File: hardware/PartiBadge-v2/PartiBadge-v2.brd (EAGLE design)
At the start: 118.9 x 117.7 mm, 31 parts, among them IC2 TSMP58000, J1 I2C, J2 Supply, U1 1042

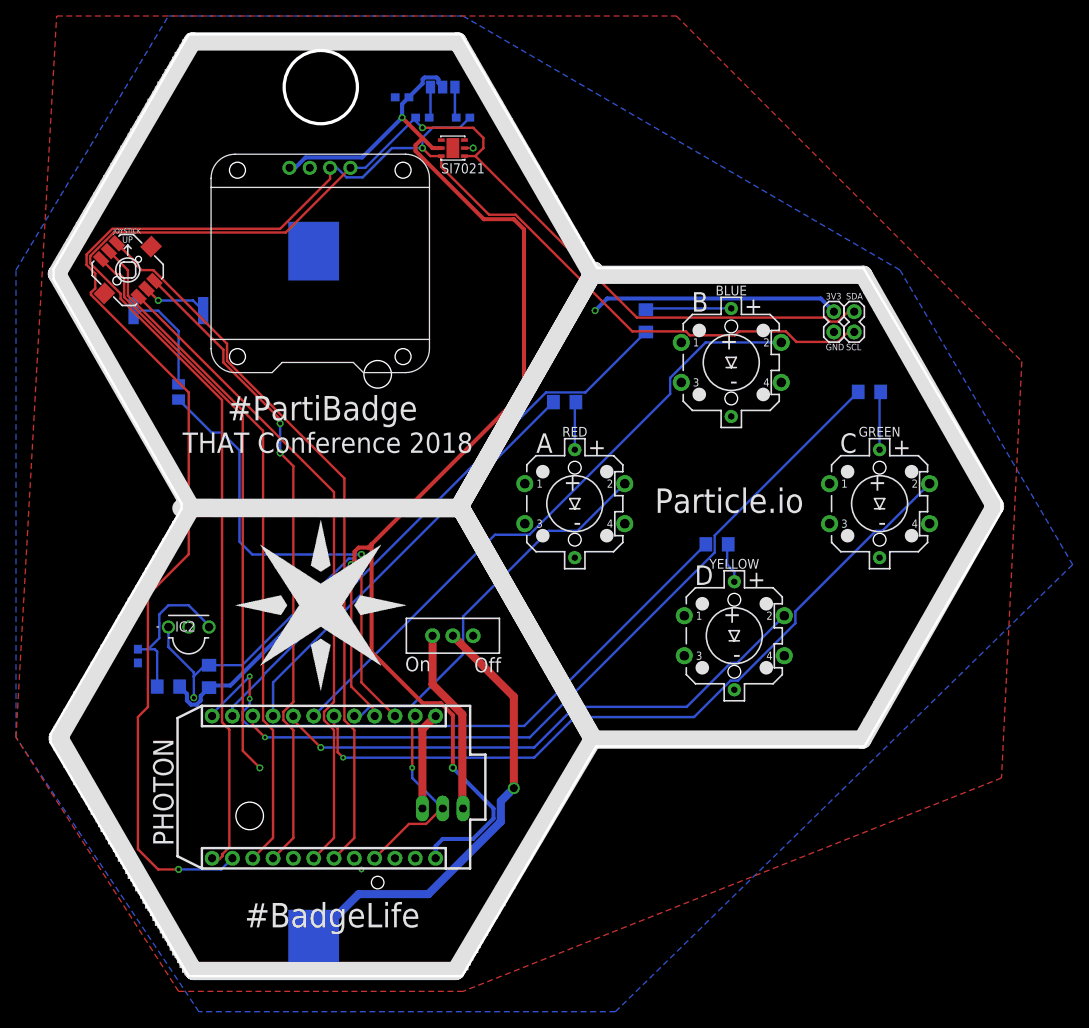
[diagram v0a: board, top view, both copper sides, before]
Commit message: updated schematic and layout based on feedback from Brett
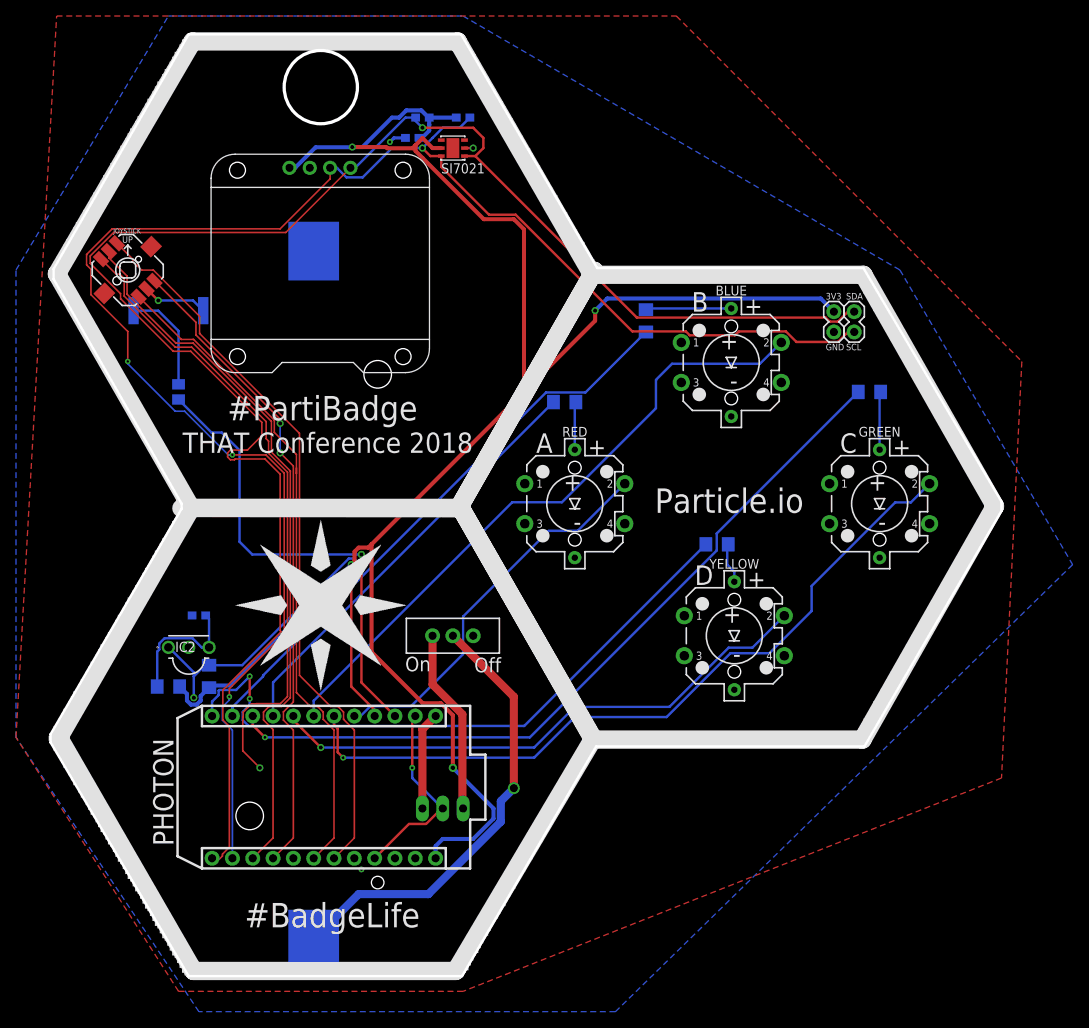
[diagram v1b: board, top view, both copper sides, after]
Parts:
- removed SJ1: (no value), jumper:SJ_2
- R7: value 100 -> 200
- moved C2 9.16 mm to (22.9, 48.3), turned to 0 degrees
- moved C1 5.24 mm to (49.5, 108.0)
- moved IC2 2.54 mm to (21.6, 45.7)
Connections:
- removed net N$11: R5.2, SJ1.3
- removed net N$12: R6.2, SJ1.1
- net +3V3: now also R5.2, R6.2; no longer SJ1.2
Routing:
- net +3V3: track 217.3 -> 237.8 mm
- net SDA: track 202.2 -> 217.0 mm
- net LEFT: track 85.1 -> 93.1 mm
- net CENT: track 85.4 -> 90.4 mm
- net SCL: track 219.4 -> 215.4 mm, vias 2 -> 4
- net N$12: track 3.88 -> 0.00 mm
- net N$11: track 3.88 -> 0.00 mm
- net N$9: track 19.8 -> 16.6 mm
- net IR_RECEIVER: track 57.9 -> 55.4 mm
- net GND: track 33.7 -> 35.8 mm, vias 3 -> 4
- net BUTTON_B: track 79.0 -> 81.0 mm
- net LED_Y: track 80.3 -> 81.6 mm
- net DOWN: track 82.4 -> 83.4 mm
- net BUTTON_G: track 94.0 -> 95.0 mm
- net UP: track 91.1 -> 91.6 mm

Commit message: additional layout tweaks
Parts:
- added D7: (no value), SparkFun-Connectors:1X01
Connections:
- new net D7: D7.1, PHOTON.20
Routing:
- net +3V3: track 237.8 -> 231.3 mm
- net D7: track 0.00 -> 6.04 mm
- net SDA: track 217.0 -> 218.5 mm
- net SCL: track 215.4 -> 216.2 mm
- net DOWN: track 83.4 -> 82.9 mm

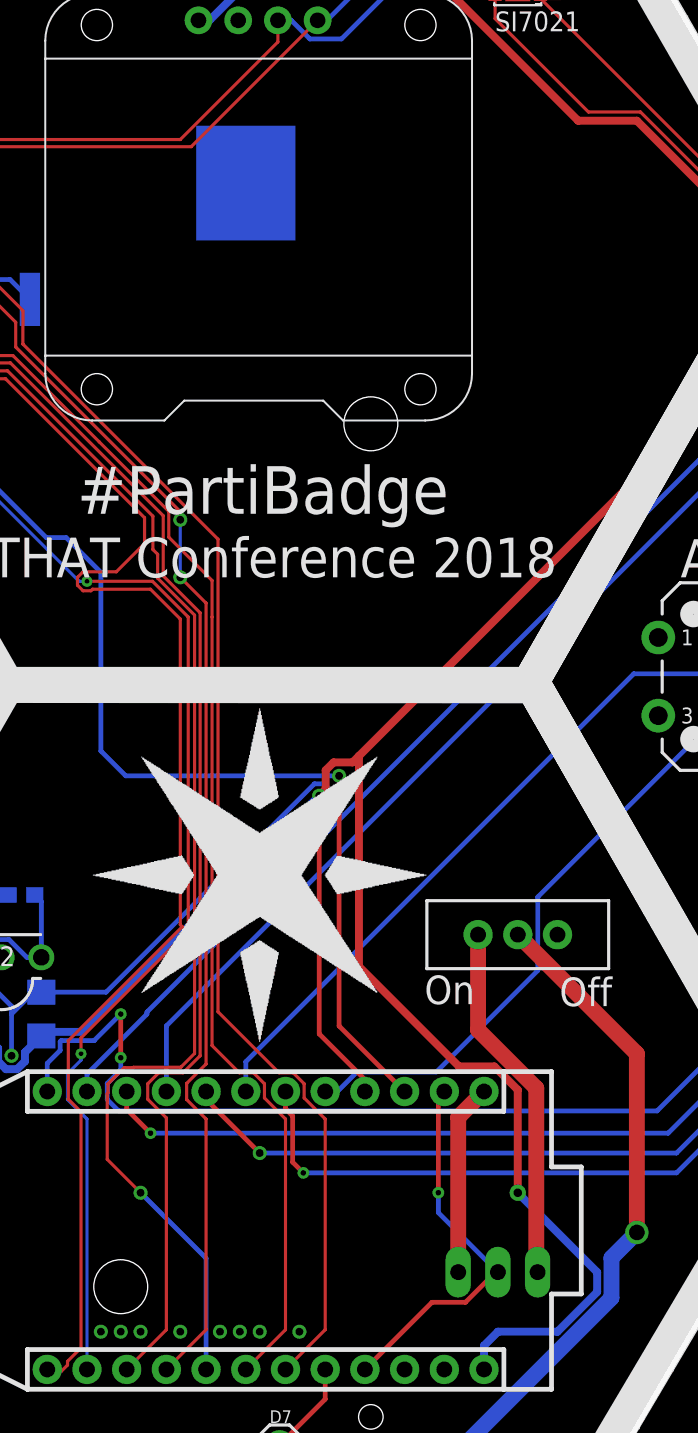
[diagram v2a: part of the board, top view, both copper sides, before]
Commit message: added vias for ground plane
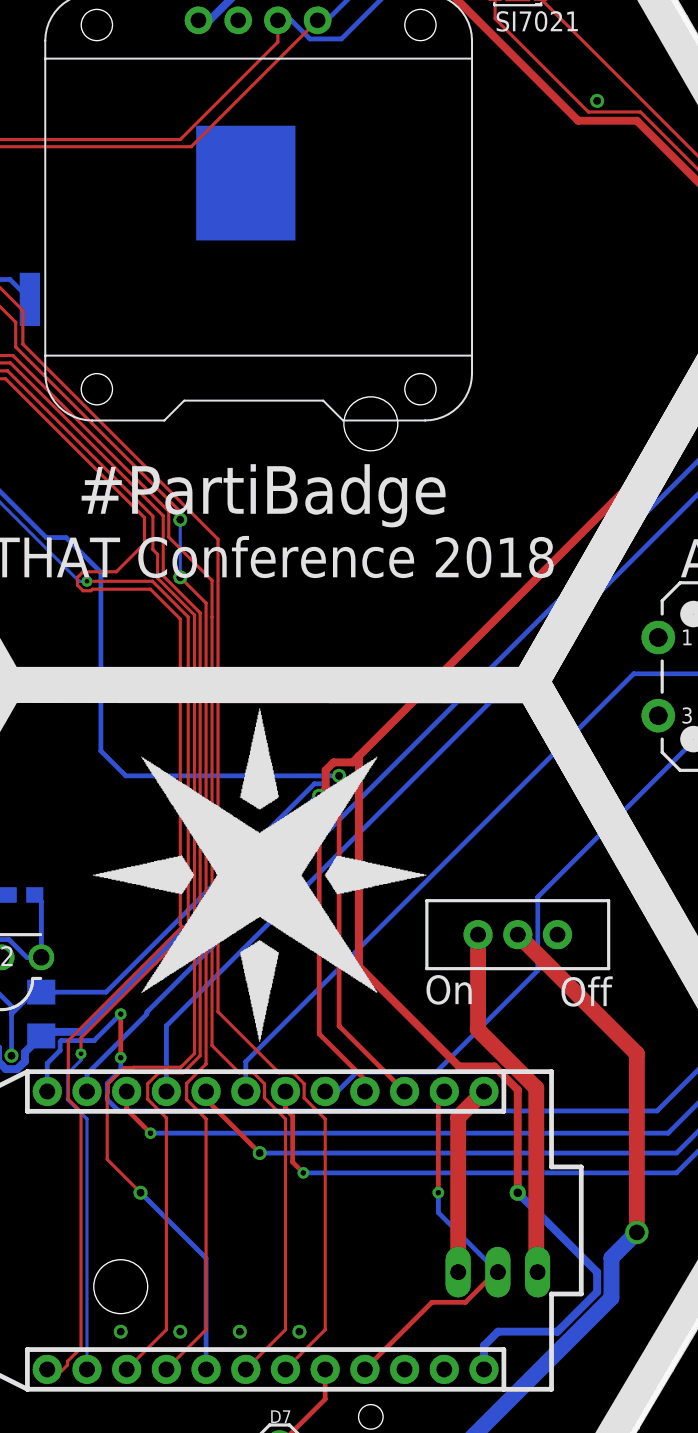
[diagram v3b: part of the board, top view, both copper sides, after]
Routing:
- net GND: vias 4 -> 9
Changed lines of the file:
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@@
 <drawing>
 <settings>
-<setting alwaysvectorfont="yes"/>
+<setting alwaysvectorfont="no"/>
 <setting verticaltext="up"/>
 </settings>
@@
 <wire x1="47.244" y1="107.95" x2="46.736" y2="107.442" width="0.4064" layer="16"/>
 <via x="46.736" y="107.442" extent="1-16" drill="0.35"/>
+<via x="29.21" y="20.32" extent="1-16" drill="0.5"/>
+<via x="33.02" y="20.32" extent="1-16" drill="0.5"/>
+<via x="36.83" y="20.32" extent="1-16" drill="0.5"/>
+<via x="40.64" y="20.32" extent="1-16" drill="0.5"/>
+<via x="59.69" y="99.06" extent="1-16" drill="0.5"/>
 </signal>
 <signal name="+3V3">
@@
 <contactref element="S5" pad="3"/>
 </signal>
-<signal name="N$2">
-<via x="27.94" y="20.32" extent="1-16" drill="0.5"/>
-</signal>
-<signal name="N$3">
-<via x="29.21" y="20.32" extent="1-16" drill="0.5"/>
-</signal>
-<signal name="N$6">
-<via x="30.48" y="20.32" extent="1-16" drill="0.5"/>
-</signal>
-<signal name="N$11">
-<via x="33.02" y="20.32" extent="1-16" drill="0.5"/>
-</signal>
-<signal name="N$12">
-<via x="35.56" y="20.32" extent="1-16" drill="0.5"/>
-</signal>
-<signal name="N$14">
-<via x="36.83" y="20.32" extent="1-16" drill="0.5"/>
-</signal>
-<signal name="N$15">
-<via x="38.1" y="20.32" extent="1-16" drill="0.5"/>
-</signal>
-<signal name="N$16">
-<via x="40.64" y="20.32" extent="1-16" drill="0.5"/>
-</signal>
 <signal name="D7">

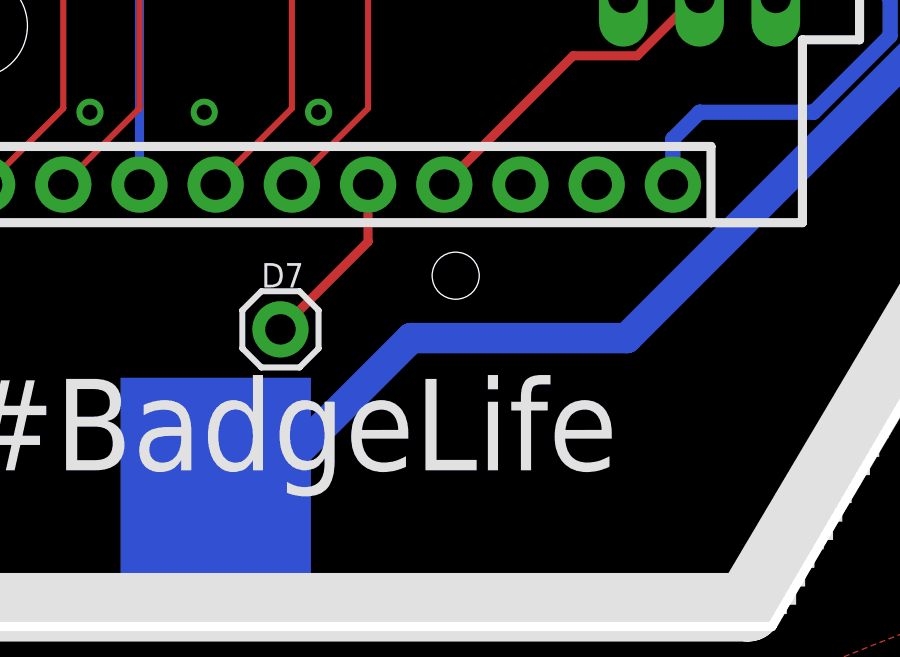
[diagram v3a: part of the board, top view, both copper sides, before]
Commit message: fix D7 breakout placement
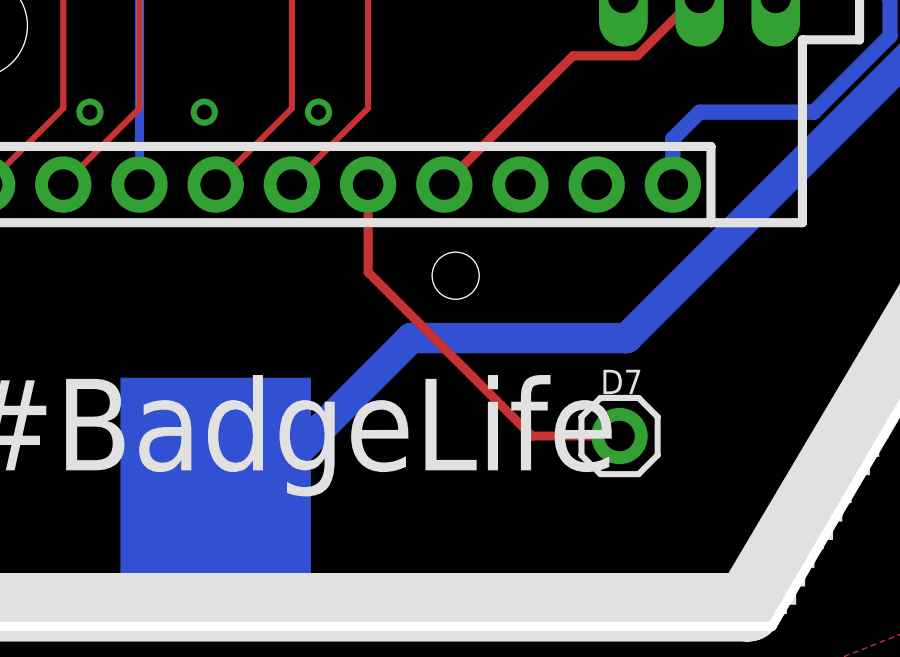
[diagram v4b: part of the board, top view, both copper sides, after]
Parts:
- R5, R6: value 4.7k -> 2.2k
- moved D7 11.8 mm to (50.7, 9.53)
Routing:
- net D7: track 6.04 -> 13.6 mm
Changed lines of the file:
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@@
 <drawing>
 <settings>
-<setting alwaysvectorfont="no"/>
+<setting alwaysvectorfont="yes"/>
 <setting verticaltext="up"/>
 </settings>
@@
 <attribute name="PROD_ID" value=" " x="87.63" y="57.15" size="1.778" layer="28" rot="MR180" display="off"/>
 </element>
-<element name="R5" library="SparkFun-Resistors" library_urn="urn:adsk.eagle:library:532" package="0603" package3d_urn="urn:adsk.eagle:package:39650/1" value="4.7k" x="50.8" y="110.49" rot="MR180">
+<element name="R5" library="SparkFun-Resistors" library_urn="urn:adsk.eagle:library:532" package="0603" package3d_urn="urn:adsk.eagle:package:39650/1" value="2.2k" x="50.8" y="110.49" rot="MR180">
 <attribute name="PROD_ID" value="RES-07857" x="50.8" y="110.49" size="1.778" layer="28" rot="MR180" display="off"/>
 </element>
-<element name="R6" library="SparkFun-Resistors" library_urn="urn:adsk.eagle:library:532" package="0603" package3d_urn="urn:adsk.eagle:package:39650/1" value="4.7k" x="55.88" y="110.49" rot="MR0">
+<element name="R6" library="SparkFun-Resistors" library_urn="urn:adsk.eagle:library:532" package="0603" package3d_urn="urn:adsk.eagle:package:39650/1" value="2.2k" x="55.88" y="110.49" rot="MR0">
 <attribute name="PROD_ID" value="RES-07857" x="55.88" y="110.49" size="1.778" layer="28" rot="MR0" display="off"/>
 </element>
@@
 <attribute name="RS_PRICE/STOCK" value="" x="37.211" y="50.8" size="1.778" layer="28" rot="MR270" display="off"/>
 </element>
-<element name="D7" library="SparkFun-Connectors" library_urn="urn:adsk.eagle:library:513" package="1X01" package3d_urn="urn:adsk.eagle:package:38028/1" value="" x="39.37" y="13.081" smashed="yes">
-<attribute name="NAME" x="38.735" y="14.478" size="0.8128" layer="25" font="vector" ratio="20"/>
-<attribute name="VALUE" x="38.1" y="11.557" size="0.6096" layer="27" font="vector" ratio="20" align="top-left"/>
+<element name="D7" library="SparkFun-Connectors" library_urn="urn:adsk.eagle:library:513" package="1X01" package3d_urn="urn:adsk.eagle:package:38028/1" value="" x="50.673" y="9.525" smashed="yes">
+<attribute name="NAME" x="50.038" y="10.922" size="0.8128" layer="25" font="vector" ratio="20"/>
+<attribute name="VALUE" x="49.403" y="8.001" size="0.6096" layer="27" font="vector" ratio="20" align="top-left"/>
 </element>
 </elements>
@@
 <contactref element="D7" pad="1"/>
 <contactref element="PHOTON" pad="20"/>
-<wire x1="39.37" y1="13.081" x2="42.291" y2="16.002" width="0.3048" layer="1"/>
-<wire x1="42.291" y1="16.002" x2="42.291" y2="17.907" width="0.3048" layer="1"/>
+<wire x1="47.752" y1="9.525" x2="42.291" y2="14.986" width="0.3048" layer="1"/>
+<wire x1="50.673" y1="9.525" x2="47.752" y2="9.525" width="0.3048" layer="1"/>
+<wire x1="42.291" y1="14.986" x2="42.291" y2="17.907" width="0.3048" layer="1"/>
 </signal>
 </signals>
